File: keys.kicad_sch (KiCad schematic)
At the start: 0 parts

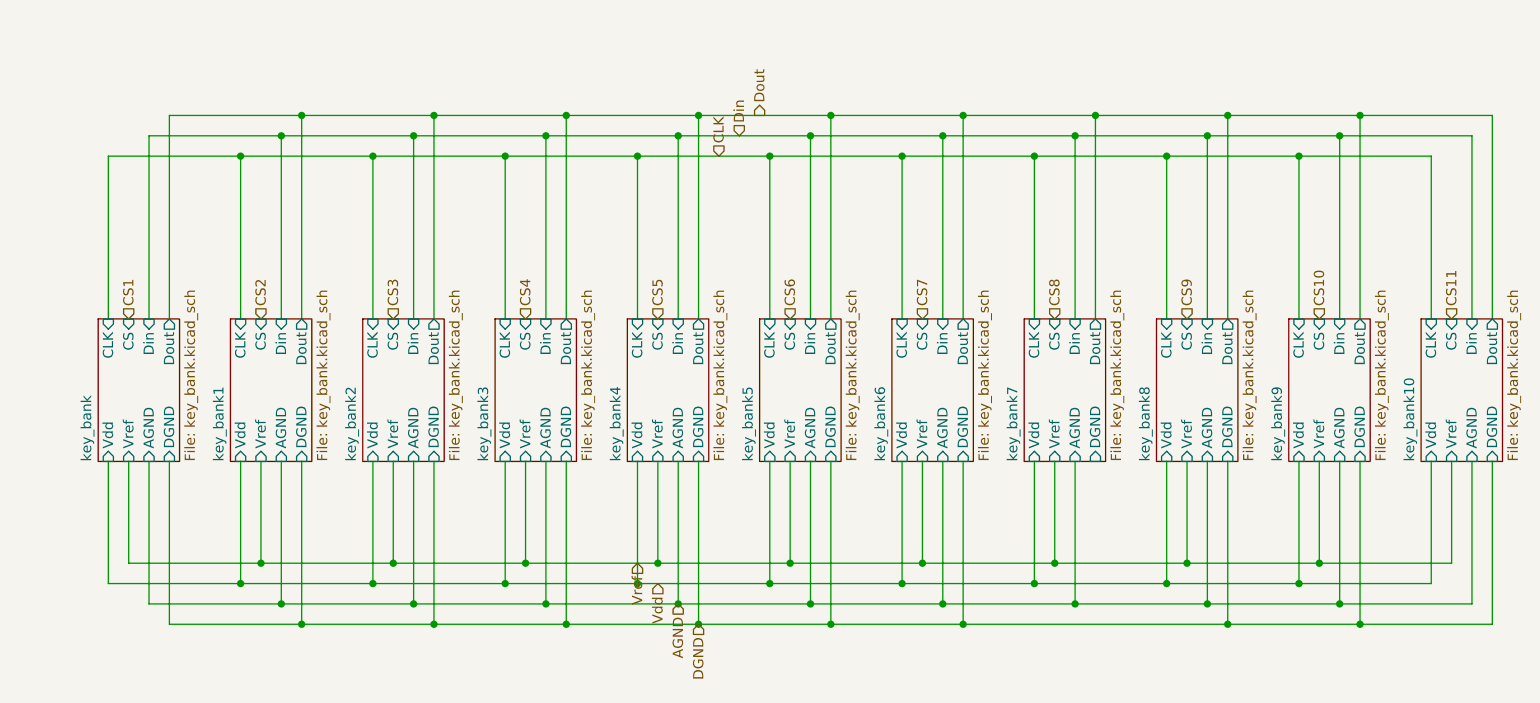
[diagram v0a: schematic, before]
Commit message: [UPDATE](TMR) switched to TMR sensors + added ldo
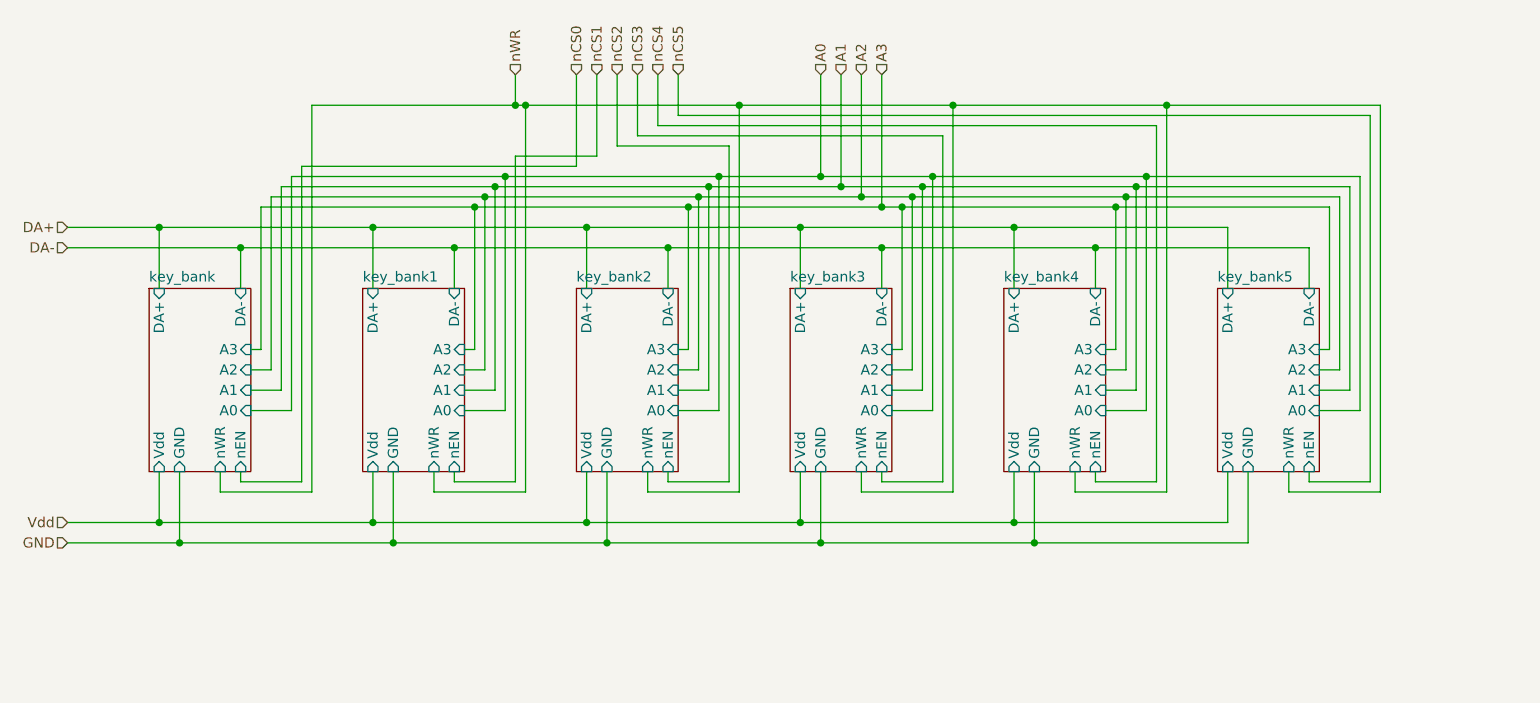
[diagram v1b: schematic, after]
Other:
- removed sheet key_bank10
- removed sheet key_bank6
- removed sheet key_bank7
- removed sheet key_bank8
- removed sheet key_bank9
- sheet key_bank ports: added A0, A1, A2, A3, DA+, DA-, GND, nEN, nWR; removed AGND, CLK, CS, DGND, Din, Dout, Vref
- sheet key_bank1 ports: added A0, A1, A2, A3, DA+, DA-, GND, nEN, nWR; removed AGND, CLK, CS, DGND, Din, Dout, Vref
- sheet key_bank2 ports: added A0, A1, A2, A3, DA+, DA-, GND, nEN, nWR; removed AGND, CLK, CS, DGND, Din, Dout, Vref
- sheet key_bank3 ports: added A0, A1, A2, A3, DA+, DA-, GND, nEN, nWR; removed AGND, CLK, CS, DGND, Din, Dout, Vref
- sheet key_bank4 ports: added A0, A1, A2, A3, DA+, DA-, GND, nEN, nWR; removed AGND, CLK, CS, DGND, Din, Dout, Vref
- sheet key_bank5 ports: added A0, A1, A2, A3, DA+, DA-, GND, nEN, nWR; removed AGND, CLK, CS, DGND, Din, Dout, Vref

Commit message: [ADD](General) v1
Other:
- company: (none) -> Ryzzen
- title: (none) -> TMR based triple USB Keyboard
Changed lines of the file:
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@@
 	(generator_version "9.0")
 	(paper "A4")
+	(title_block
+		(title "TMR based triple USB Keyboard")
+		(date "2025-12-28")
+		(rev "v1")
+		(company "Ryzzen")
+	)
 	(junction
 		(at 194.31 82.55)
@@
 			(project "RyzzenKeyboard"
 				(path "/5d44d704-6136-40a8-98a4-93f001ea8743/c5dd3d76-8c7d-4253-bbc0-6b560edbfa92"
-					(page "4")
+					(page "108")
 				)
 			)
@@
 			(project "RyzzenKeyboard"
 				(path "/5d44d704-6136-40a8-98a4-93f001ea8743/c5dd3d76-8c7d-4253-bbc0-6b560edbfa92"
-					(page "2")
-				)
-			)
+					(page "4")
+				)
+			)

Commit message: [ADD](General) v2 split
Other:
- removed sheet key_bank
- removed sheet key_bank1
- removed sheet key_bank4
- removed sheet key_bank5
